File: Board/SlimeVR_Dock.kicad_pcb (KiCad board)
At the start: 2 copper layers, 100 x 78.3 mm, 119 parts, among them J1Fan1 Conn_01x04_Pin, J1Temp1 Conn_01x05_Pin, J1_Control1 Conn_01x03_Pin, J1_MainPW1 USB_C_Receptacle_USB2.0_16P, J1_Monitor1 Conn_01x03_Pin, J1_Prog1 Conn_01x03_Pin, J2 USB_C_Receptacle_USB2.0_16P, J3 USB_C_Receptacle_USB2.0_16P, J4 USB_C_Receptacle_USB2.0_16P, J5 USB_C_Receptacle_USB2.0_16P, J6 USB_C_Receptacle_USB2.0_16P, J7 USB_C_Receptacle_USB2.0_16P, J8 USB_C_Receptacle_USB2.0_16P, J9 USB_C_Receptacle_USB2.0_16P, Q1 NDT452AP, Q2 BC857, Q3 BC857, Q4 BC857, Q5 BC857, Q6 BC817, U1 ESP32-C3-WROOM-02, U10 INA226, U11 AP22652W6-7, U12 INA226, U13 INA226, U14 AP22652W6-7, U15 INA226, U16 INA226, U17 74HC165, U18 74HC165, U19 74HC595, U2 CH224K, U3 XC6220B331MR, U4 TPS548A20RVER, U5 AP22652W6-7, U6 INA226, U7 INA226, U8 AP22652W6-7, U9 INA226

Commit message: Version 2
- Fixed StepDown stabilization 5V output - probebly idk :D
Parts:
- added 20V: TestPoint_Pad_1.5x1.5mm, TestPoint:TestPoint_Pad_1.5x1.5mm, F.Cu at (106.0, 104.3)
- added 3V3: TestPoint_Pad_1.5x1.5mm, TestPoint:TestPoint_Pad_1.5x1.5mm, F.Cu at (101.0, 71.4)
- added 5V: TestPoint_Pad_1.5x1.5mm, TestPoint:TestPoint_Pad_1.5x1.5mm, F.Cu at (119.6, 83.9)
- added C31: 47uF, Capacitor_SMD:C_0805_2012Metric, B.Cu at (116.6, 86.0)
- added GND: TestPoint_Pad_1.5x1.5mm, TestPoint:TestPoint_Pad_1.5x1.5mm, F.Cu at (122.1, 92.5)
- C24, C25: value 47uF -> 100uF; footprint Capacitor_SMD:C_0805_2012Metric -> Capacitor_SMD:C_Elec_6.3x5.4
- C26: moved to B.Cu
- R36: value 100k -> 1n
- moved C25 7.97 mm to (105.7, 77.6)
- moved C26 6.65 mm to (114.6, 86.0), turned to -90 degrees
- moved C24 3.62 mm to (112.8, 77.6)
- moved R23 2.92 mm to (111.7, 72.2)
- moved R24 2.69 mm to (107.1, 72.2)
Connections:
- U4 pad V: Earth -> (no net)
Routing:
- net SDA: track 261.5 -> 265.0 mm
- net SCL: track 233.6 -> 236.6 mm
- net 5VStepDwon: track 145.4 -> 142.8 mm, vias 9 -> 12
- net VBUS: track 27.3 -> 29.0 mm
- net Earth: vias 118 -> 117
- added copper zone on B.Cu, net 5VStepDwon
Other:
- board text added: "Ver.: 2"
- board text removed: "Ver.: 1"

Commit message: Fix Layout
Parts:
- added 20V: TestPoint_Pad_1.5x1.5mm, TestPoint:TestPoint_Pad_1.5x1.5mm, F.Cu at (114.8, 101.8)
- moved GND 15.5 mm to (106.7, 91.1)
- moved 5V 14.7 mm to (104.9, 83.3)
- moved C25 1.22 mm to (104.5, 77.8)
- moved C24 1.22 mm to (111.7, 77.8)
- renumbered 20V to USB
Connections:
- U4 pad V: (no net) -> Earth
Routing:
- net /StepDown/Vin: track 10.0 -> 11.3 mm
- net 5VStepDwon: track 142.8 -> 143.8 mm
- net Earth: vias 117 -> 118
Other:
- board text added: "DO NOT CUT ANYTHING"
- board text removed: "DO NOT CUT ANYTHINK"

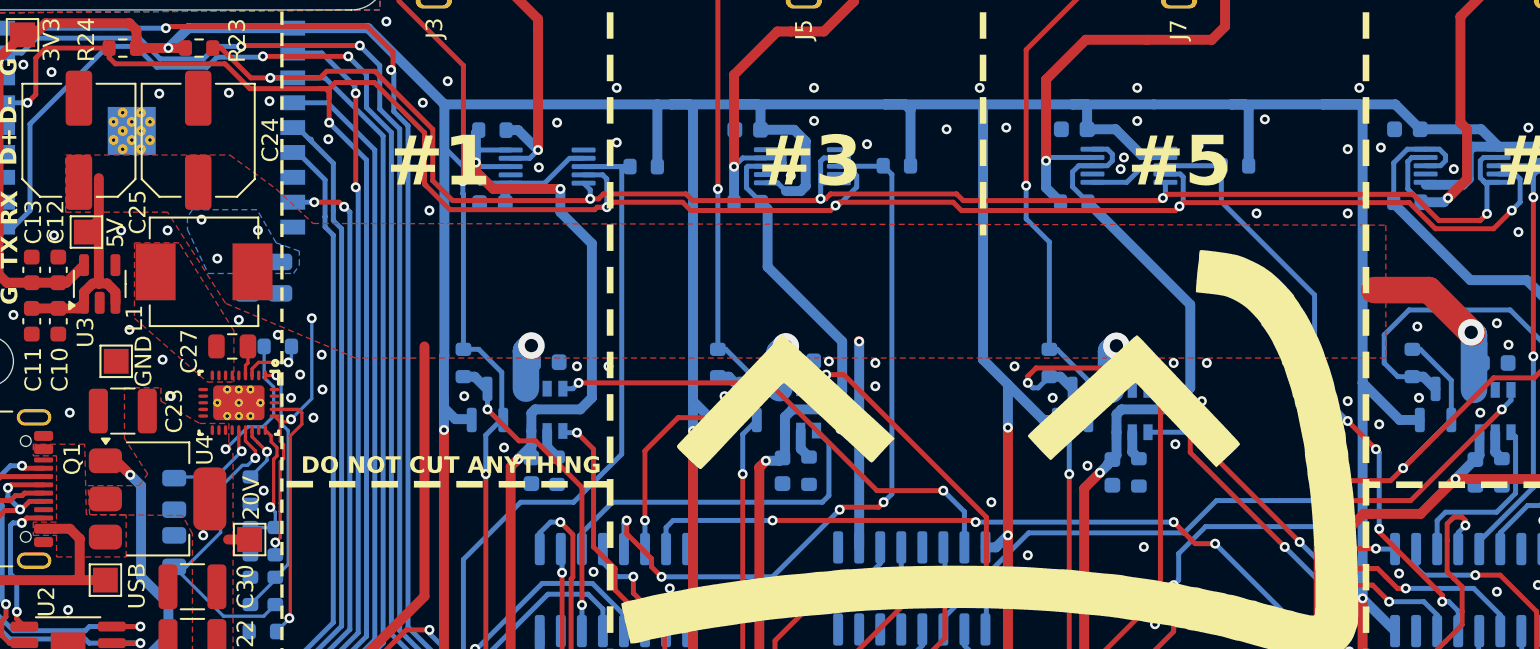
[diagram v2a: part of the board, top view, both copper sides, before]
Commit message: Fixed CC_detect transistor
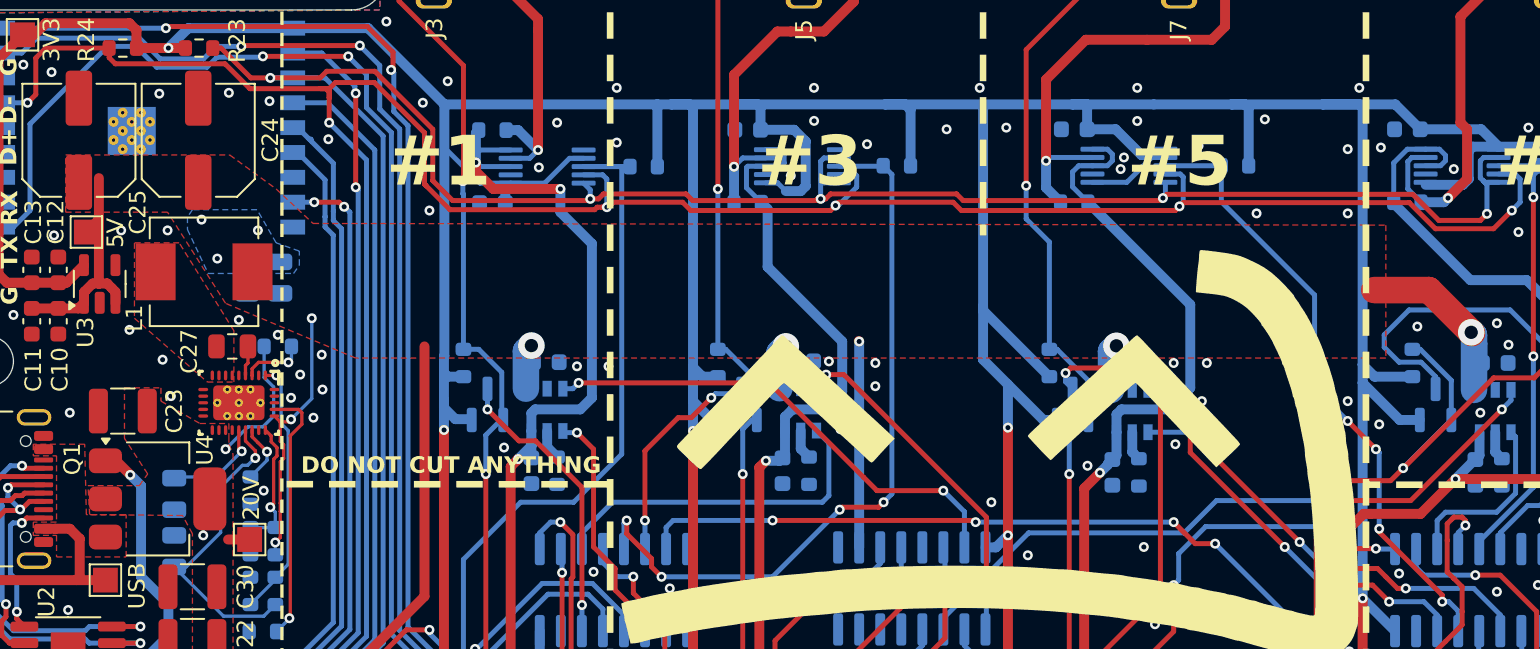
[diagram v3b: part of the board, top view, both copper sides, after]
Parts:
- removed GND: TestPoint_Pad_1.5x1.5mm, TestPoint:TestPoint_Pad_1.5x1.5mm
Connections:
- R11 pad 1: CC2 -> +3V3
- R14 pad 1: CC3 -> +3V3
- R5 pad 1: CC0 -> +3V3
- R8 pad 1: CC1 -> +3V3
- U4 pad V: Earth -> (no net)
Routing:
- net +3V3: track 473.7 -> 485.9 mm
- net CC2: track 37.7 -> 32.7 mm
- net CC1: track 15.8 -> 13.3 mm
- net CC0: track 19.2 -> 17.6 mm
- net Earth: vias 118 -> 113

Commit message: fixed grounding and updated to kicad 10
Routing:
- net Earth: vias 113 -> 116

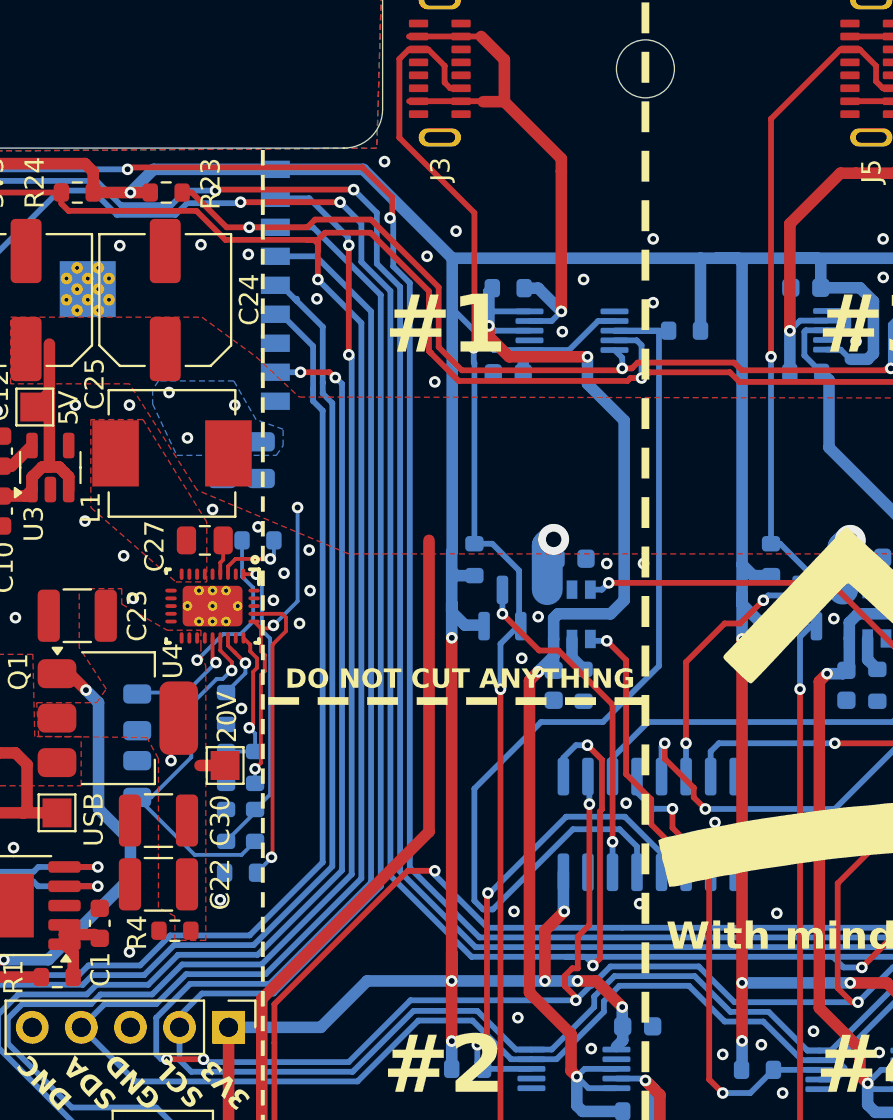
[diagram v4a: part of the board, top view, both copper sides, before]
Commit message: DRC fix
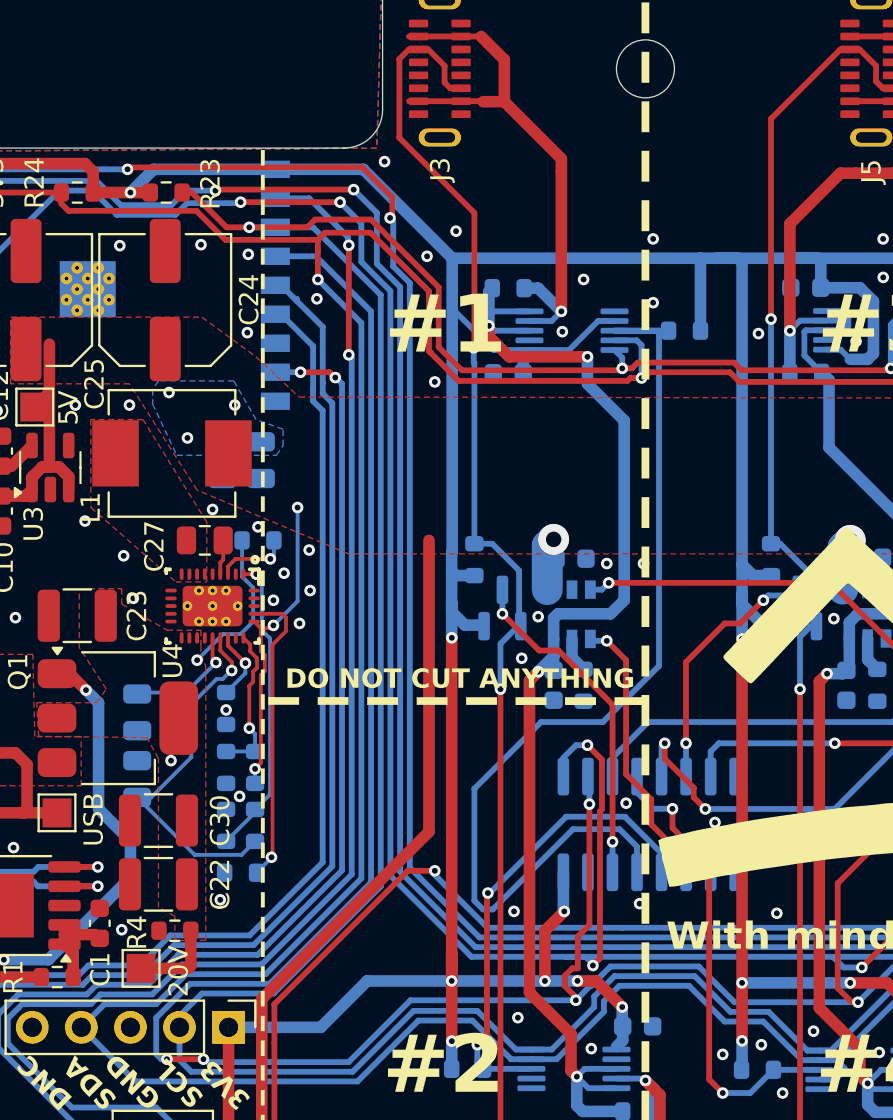
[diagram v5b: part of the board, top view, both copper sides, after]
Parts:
- moved 20V 11.4 mm to (110.4, 112.3)
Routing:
- net /StepDown/Vin: track 11.3 -> 14.5 mm
- net SDA: track 264.9 -> 264.0 mm
- net Earth: vias 116 -> 119
